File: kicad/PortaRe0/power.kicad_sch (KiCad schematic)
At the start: 43 parts, among them J4 Conn_01x02_Socket, SW1 SW_START, SW2 KillSW, U1 BQ25895RTWR, U2 TPS61023DRLR, U3 AP2112K-3.3TRG1

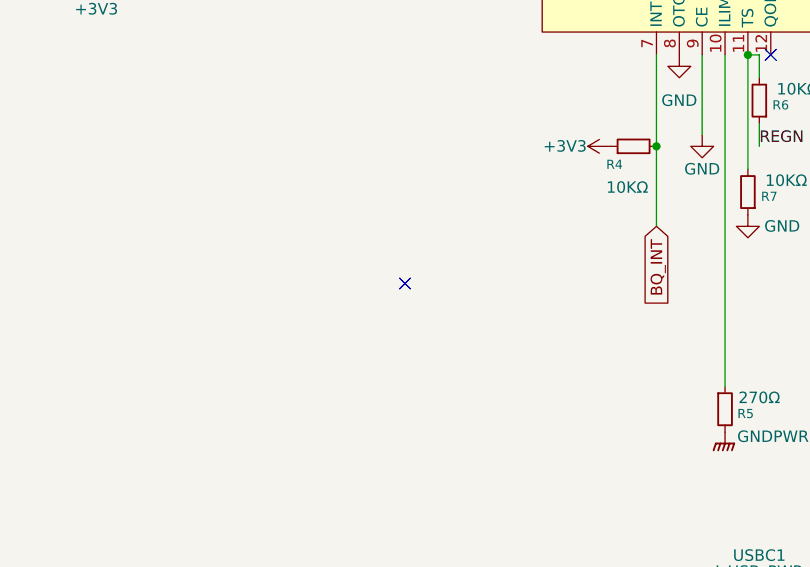
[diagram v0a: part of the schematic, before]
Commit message: KiCad/Docs: チェックシート04-06完了・回路修正(session25)
- VL812: W25Q32 /CS GNDプルダウン→3V3_HUBプルアップ修正
- RP2040 #1/#2: クリスタルシンボル GND23→GND24 修正
- RP2040 #1: GP24/GP25 接続追加
- チェックシート04(VL812)/05(RP2040 kbd)/06(RP2040 audio)記入完了

Co-Authored-By: Claude Sonnet 4.6 <noreply@anthropic.com>
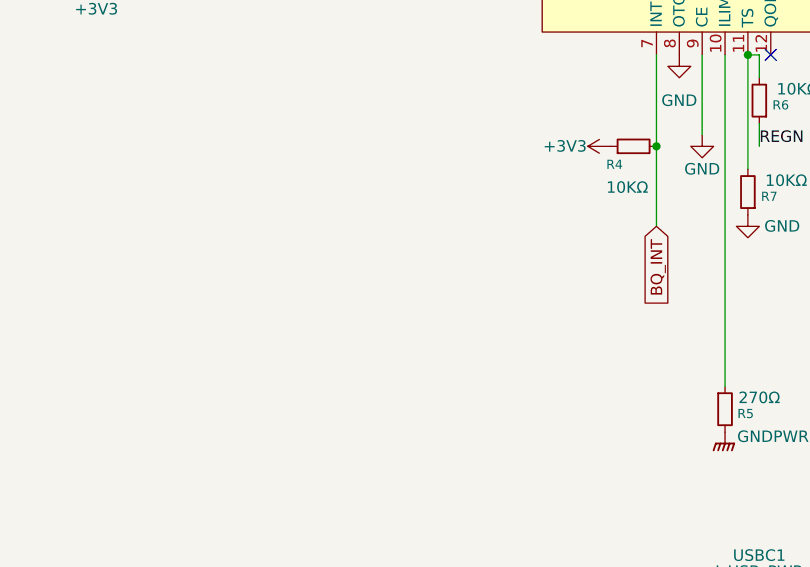
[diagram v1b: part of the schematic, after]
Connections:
- no-connect marks 8 -> 7
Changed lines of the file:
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@@
 		(at 300.99 45.72)
-	)
-	(no_connect
-		(at 66.04 124.46)
 	)
 	(wire

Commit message: KiCad: 未コミットの回路図変更を追加
Co-Authored-By: Claude Sonnet 4.6 <noreply@anthropic.com>
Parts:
- C10: value 22µF -> 22μF
- C109, C12, C13, C6, C8: value 10µF -> 10μF
- R1, R2, R4, R6, R7: value 10KΩ -> 10kΩ
- R48, R49: value 5.1KΩ -> 5.1kΩ
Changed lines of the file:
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@@
 			)
 		)
-		(property "Value" "10µF"
+		(property "Value" "10μF"
 			(at 315.468 86.106 0)
 			(effects
@@
 			)
 		)
-		(property "Value" "10KΩ"
+		(property "Value" "10kΩ"
 			(at 30.988 85.598 0)
 			(effects
@@
 			)
 		)
-		(property "Value" "10KΩ"
+		(property "Value" "10kΩ"
 			(at 88.392 113.792 90)
 			(effects
@@
 			)
 		)
-		(property "Value" "5.1KΩ"
+		(property "Value" "5.1kΩ"
 			(at 92.71 167.64 90)
 			(effects
@@
 			)
 		)
-		(property "Value" "5.1KΩ"
+		(property "Value" "5.1kΩ"
 			(at 92.71 182.88 90)
 			(effects
@@
 			)
 		)
-		(property "Value" "10µF"
+		(property "Value" "10μF"
 			(at 94.488 43.434 0)
 			(effects
@@
 			)
 		)
-		(property "Value" "10µF"
+		(property "Value" "10μF"
 			(at 225.298 117.856 0)
 			(effects
@@
 			)
 		)
-		(property "Value" "10KΩ"
+		(property "Value" "10kΩ"
 			(at 110.744 113.03 0)
 			(effects
@@
 			)
 		)
-		(property "Value" "10KΩ"
+		(property "Value" "10kΩ"
 			(at 32.512 79.756 0)
 			(effects
@@
 			)
 		)
-		(property "Value" "10KΩ"
+		(property "Value" "10kΩ"
 			(at 112.014 102.87 0)
 			(effects
@@
 			)
 		)
-		(property "Value" "10µF"
+		(property "Value" "10μF"
 			(at 189.738 117.856 0)
 			(effects
@@
 			)
 		)
-		(property "Value" "10µF"
+		(property "Value" "10μF"
 			(at 283.718 61.976 0)
 			(effects
@@
 			)
 		)
-		(property "Value" "22µF"
+		(property "Value" "22μF"
 			(at 358.394 67.056 0)
 			(effects

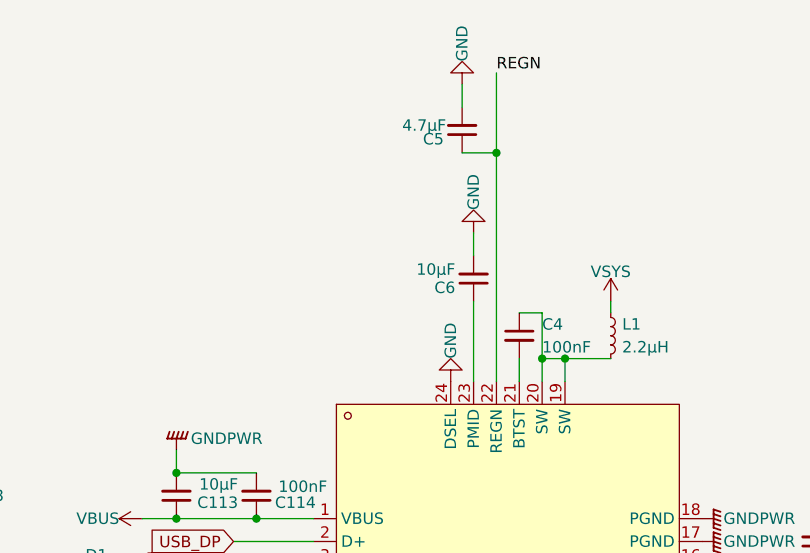
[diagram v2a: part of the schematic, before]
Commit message: Docs/KiCad: session29終了処理・LED/スイッチ確定・audio/power修正
Co-Authored-By: Claude Sonnet 4.6 <noreply@anthropic.com>
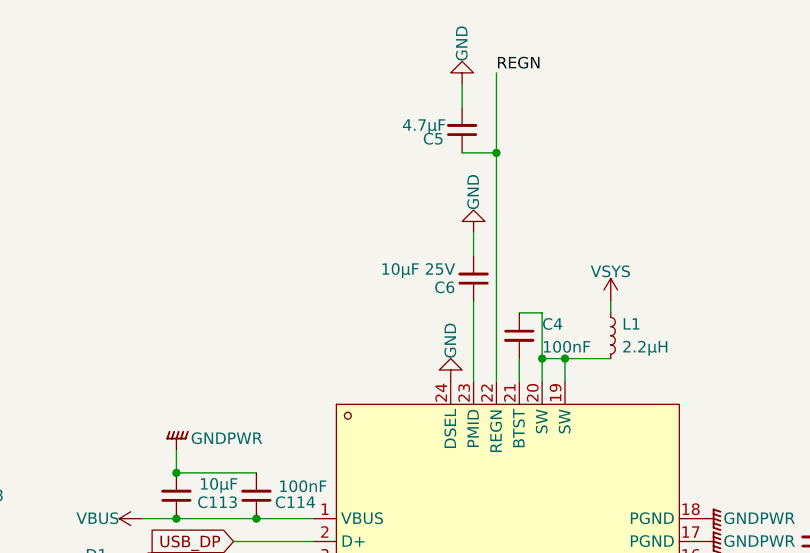
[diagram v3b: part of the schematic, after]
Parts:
- C6: value 10μF -> 10μF 25V
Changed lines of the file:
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@@
 			)
 		)
-		(property "Value" "10μF"
+		(property "Value" "10μF 25V"
 			(at 94.488 43.434 0)
 			(effects

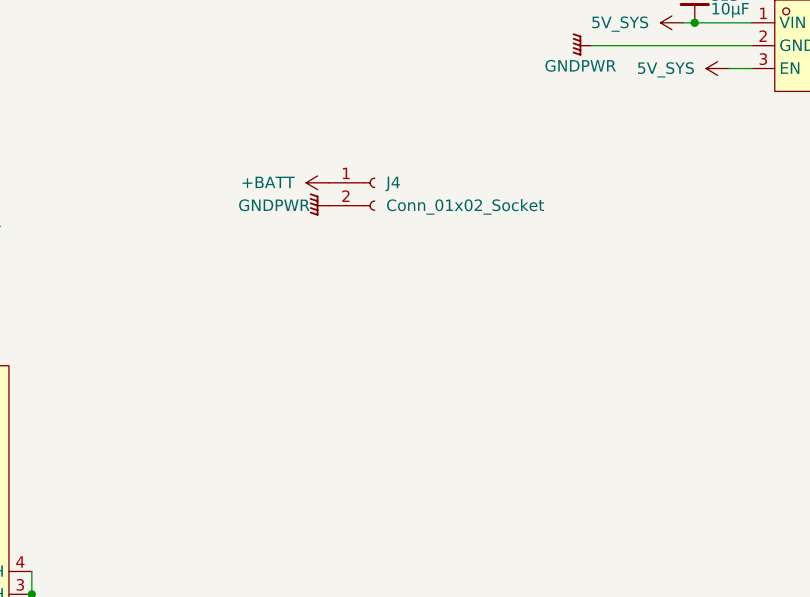
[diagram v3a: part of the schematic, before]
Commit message: KiCad/Docs: session30終了処理・フットプリント割り当て完了・コネクタ確定
- フットプリント全割り当て完了（全シート）
- 新規フットプリント追加: SKSCLBE010/SKRPABE010/クリスタル/インダクタ×3/JST PHコネクタ×2
- コネクタ確定: バッテリー=B8B-PH-K-S(C157974) / SPK+FAN=B2B-PH-K-S(C131337)
- J5(hdmi_adapter): PinHeader_2x08_P2.00mm_Vertical
- Claude.md: ファン制御 RP2040 #1 GP26→BSS138→J6 に更新
- passive_parts.txt: コネクタセクション追加

Co-Authored-By: Claude Sonnet 4.6 <noreply@anthropic.com>
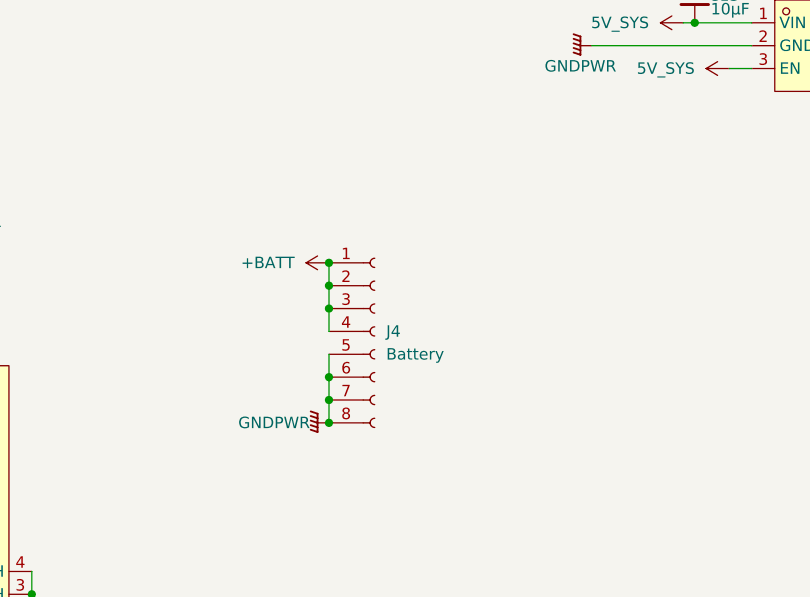
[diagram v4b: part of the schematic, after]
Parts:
- removed J4: Conn_01x02_Socket, symbol Connector:Conn_01x02_Socket
- added J4: Battery, PortaRe0:CONN-TH_B8B-PH-K-S-LF-SN, symbol Connector:Conn_01x08_Socket
- C1, C10, C109, C11, C110, C113, C114, C12, C13, C2, C3, C4, C5, C6, C7, C8, C9: footprint (none) -> Capacitor_SMD:C_0603_1608Metric
- D1: footprint (none) -> LED_SMD:LED_0603_1608Metric
- L1: footprint (none) -> PortaRe0:IND-SMD_L4.4-W4.2
- L2: footprint (none) -> PortaRe0:IND-SMD_L3.2-W2.5_CKST322512-2.2UH
- R1, R10, R11, R14, R2, R21, R3, R4, R48, R49, R5, R6, R7, R9: footprint (none) -> Resistor_SMD:R_0603_1608Metric
- SW1: footprint (none) -> PortaRe0:KEY-SMD_4P-SKSCLXX010
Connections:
- net +BATT: now also J4.1 (Pin_1), J4.2 (Pin_2), J4.3 (Pin_3), J4.4 (Pin_4)
- net GND: now also J4.5 (Pin_5), J4.6 (Pin_6), J4.7 (Pin_7), J4.8 (Pin_8)

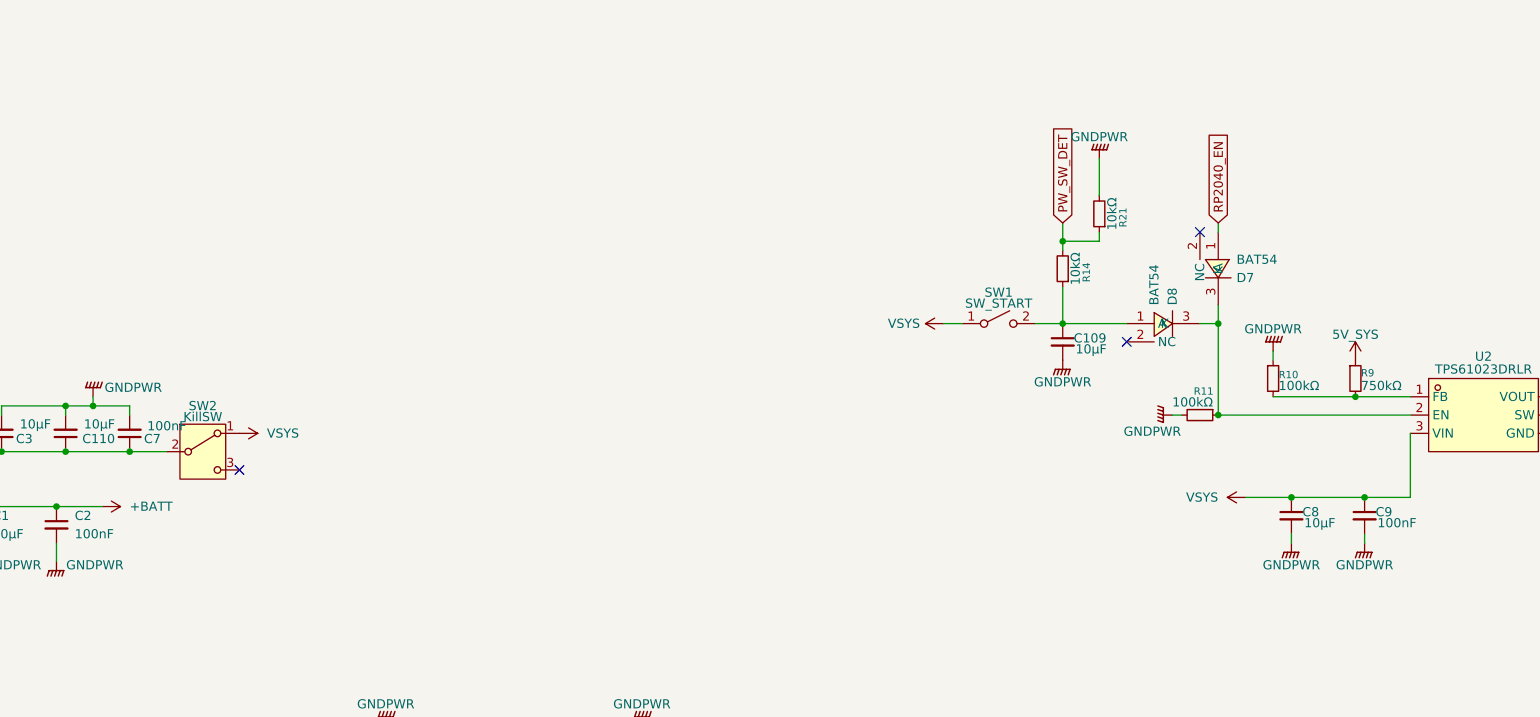
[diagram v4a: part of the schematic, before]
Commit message: Docs/KiCad: session31終了処理・PROGRESS/index更新
- キルスイッチ確定: MSK12C02(C431540) EN制御方式・KiCad配線完了
- ヘッドフォンジャック確定: PJ-307C(C16684) TH / 配線・pull-up完了
- J4バッテリーコネクタ: S8B-PH-K-S-LF-SN(C157915) 水平型確定
- BOM Y4フットプリント修正
- 新規ライブラリ追加: MSK12C02/PJ-307C/S8B-PH-K-S他
- Phase 2 回路設計 全シート完了

Co-Authored-By: Claude Sonnet 4.6 <noreply@anthropic.com>
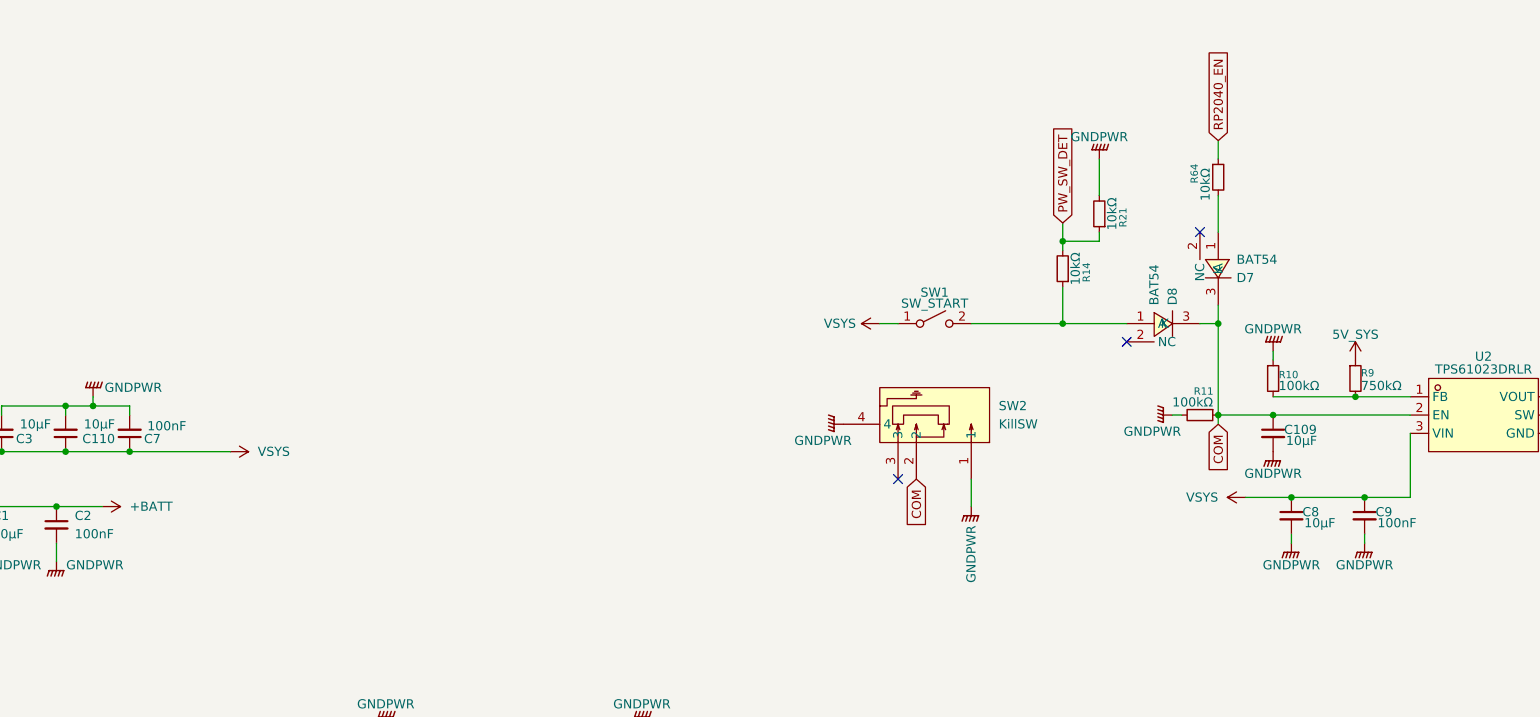
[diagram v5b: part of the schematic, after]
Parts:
- removed SW2: KillSW, symbol Switch:SW_SPDT
- added R64: 10kΩ, Resistor_SMD:R_0603_1608Metric, symbol Device:R_Small
- added SW2: KillSW, PortaRe0:SW-TH_MSK12C02, symbol PortaRe0:MSK12C02
- J4: footprint PortaRe0:CONN-TH_B8B-PH-K-S-LF-SN -> PortaRe0:CONN-TH_S8B-PH-K-S-LF-SN
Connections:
- net GND: now also SW2.1, SW2.4
- net RP2040_EN: now also R64.1; no longer D7.1 (A)
- net VSYS: now also C110.1, C3.1, C7.1, U1.15 (SYS), U1.16 (SYS)
- net COM: now reaches D7.3 (K), D8.3 (K), R11.1, U2.2 (EN)
- net COM: now also C109.1, SW2.2
- net at D8.1 (A), R14.1, SW1.2 (B): no longer C109.1
- new net: D7.1 (A), R64.2
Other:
- moved on the sheet: C109, SW1
